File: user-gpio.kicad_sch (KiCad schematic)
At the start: 70 parts, among them J13 61232020621, J14 62704020621, J15 62703420621, J4 PMOD-2x6-artyA7_spacing, J5 PMOD-2x6-artyA7_spacing, Q10 BSS138PW, Q11 BSS138PW, Q12 BSS138PW, Q13 BSS138PW, Q14 BSS138PW, Q15 BSS138PW, Q8 BSS138PW, Q9 BSS138PW, SW2 CVS-08TB

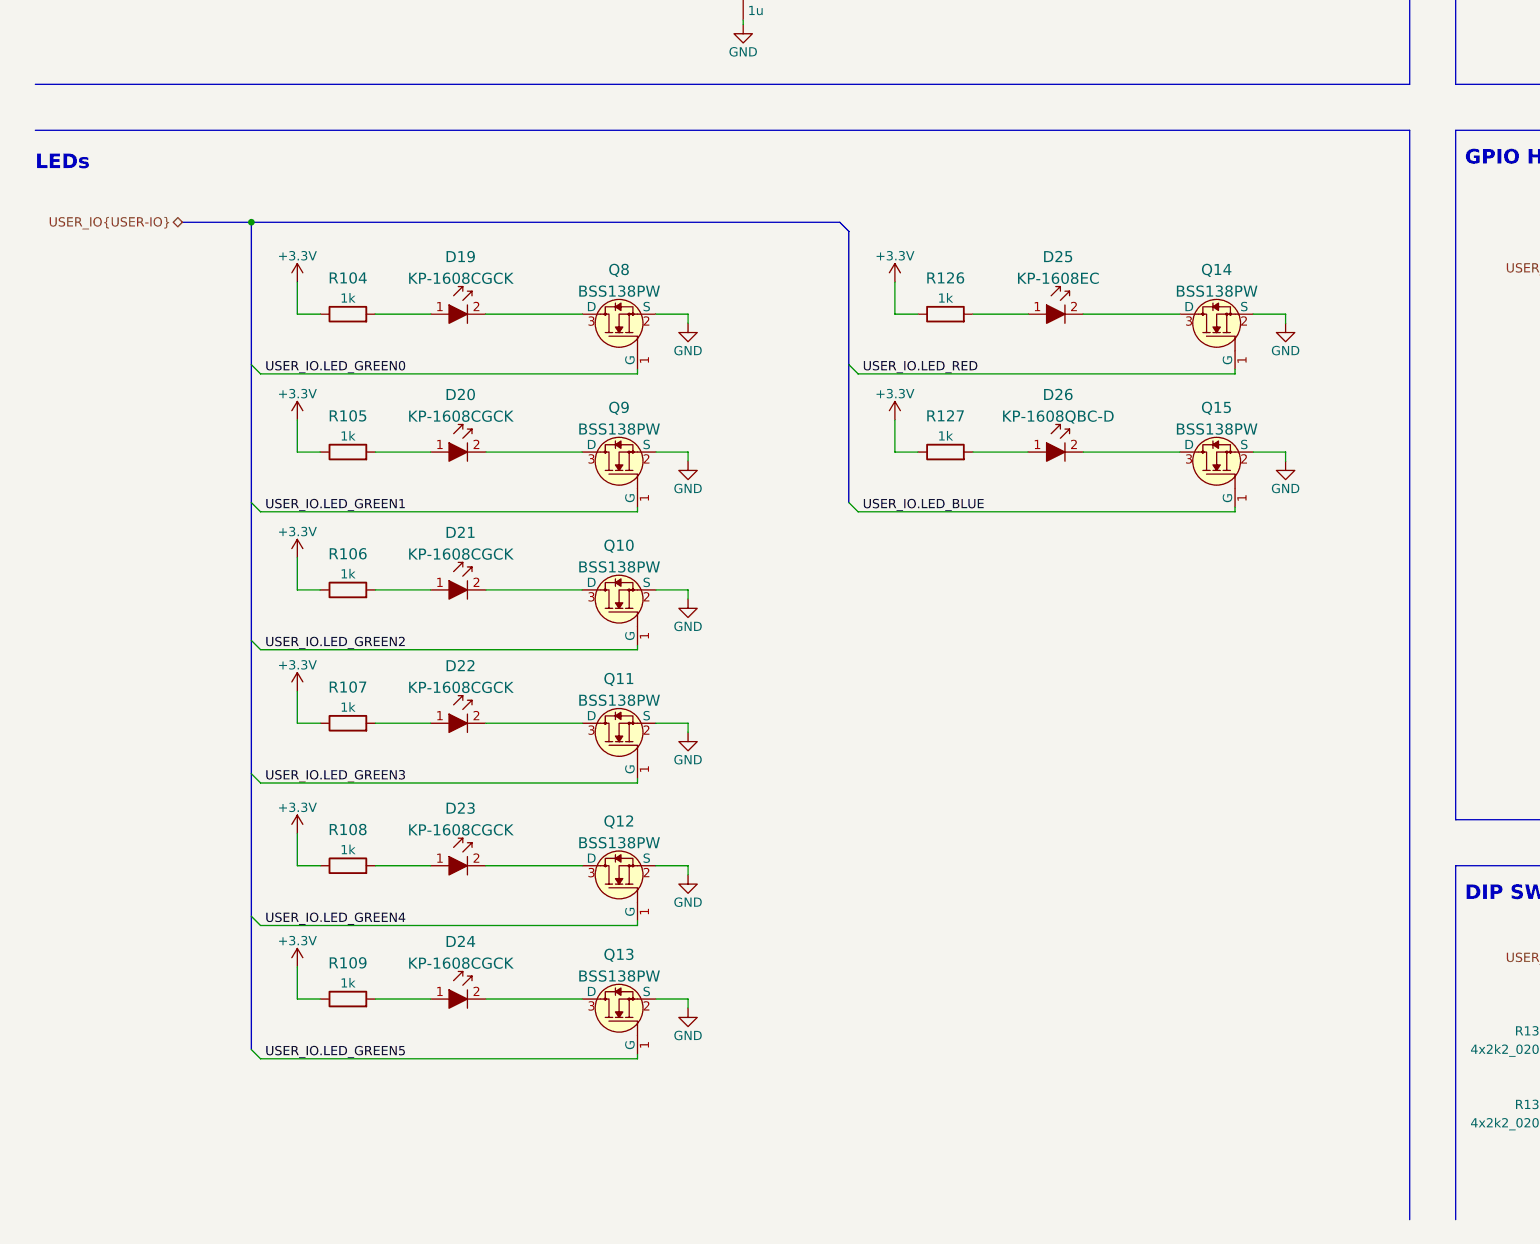
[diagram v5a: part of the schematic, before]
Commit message: Add fan headers
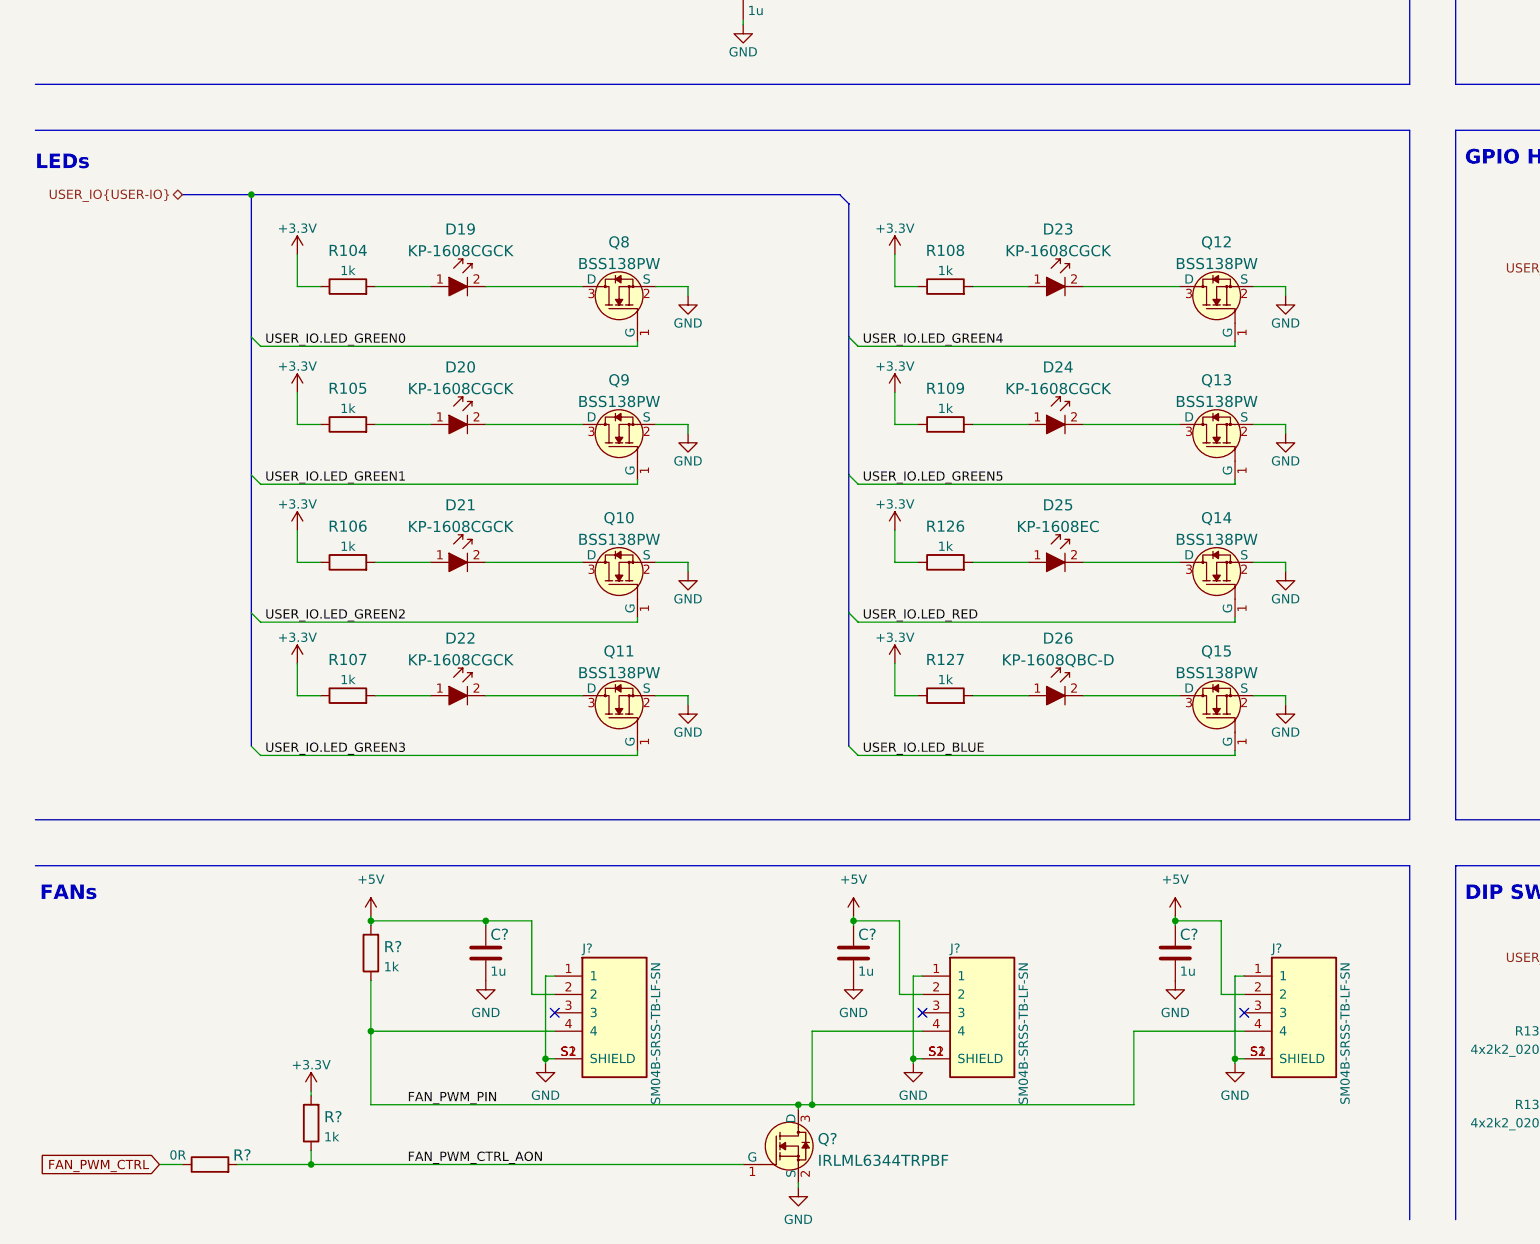
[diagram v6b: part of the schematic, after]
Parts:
- added C? (x3): C_1u_0402, antmicro-footprints:0402-cap, symbol antmicroCapacitors0402:C_1u_0402
- added J? (x3): SM04B-SRSS-TB-LF-SN, antmicro-footprints:SM04B-SRSS-TB-LF-SN, symbol antmicroRectangularConnectorsHeadersMalePins:SM04B-SRSS-TB-LF-SN
- added Q?: IRLML6344TRPBF, antmicro-footprints:SOT-23-3, symbol antmicroTransistorsFETsMOSFETsSingle:IRLML6344TRPBF
- added R?: R_0R_0402, antmicro-footprints:0402-res, symbol antmicroResistors0402:R_0R_0402
- added R? (x2): R_1k_0402, antmicro-footprints:0402-res, symbol antmicroResistors0402:R_1k_0402
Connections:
- net +3V3: now also R?.2
- net GND: now also C?.2, C?.2, C?.2, J?.1, J?.1, J?.1, J?.S1 (SHIELD), J?.S1 (SHIELD), J?.S1 (SHIELD), J?.S2 (SHIELD), J?.S2 (SHIELD), J?.S2 (SHIELD), Q?.2 (S)
- new net +5V: C?.1, C?.1, C?.1, J?.2, J?.2, J?.2, R?.2
- new net FAN_PWM_CTRL: R?.1
- new net FAN_PWM_CTRL_AON: Q?.1 (G), R?.1, R?.2
- new net FAN_PWM_PIN: J?.4, J?.4, J?.4, Q?.3 (D), R?.1
- no-connect marks 4 -> 7
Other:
- note added: "FANs"
- moved on the sheet: D19, D20, D21, D22, D23, D24, D25, D26, Q10, Q11, Q12, Q13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

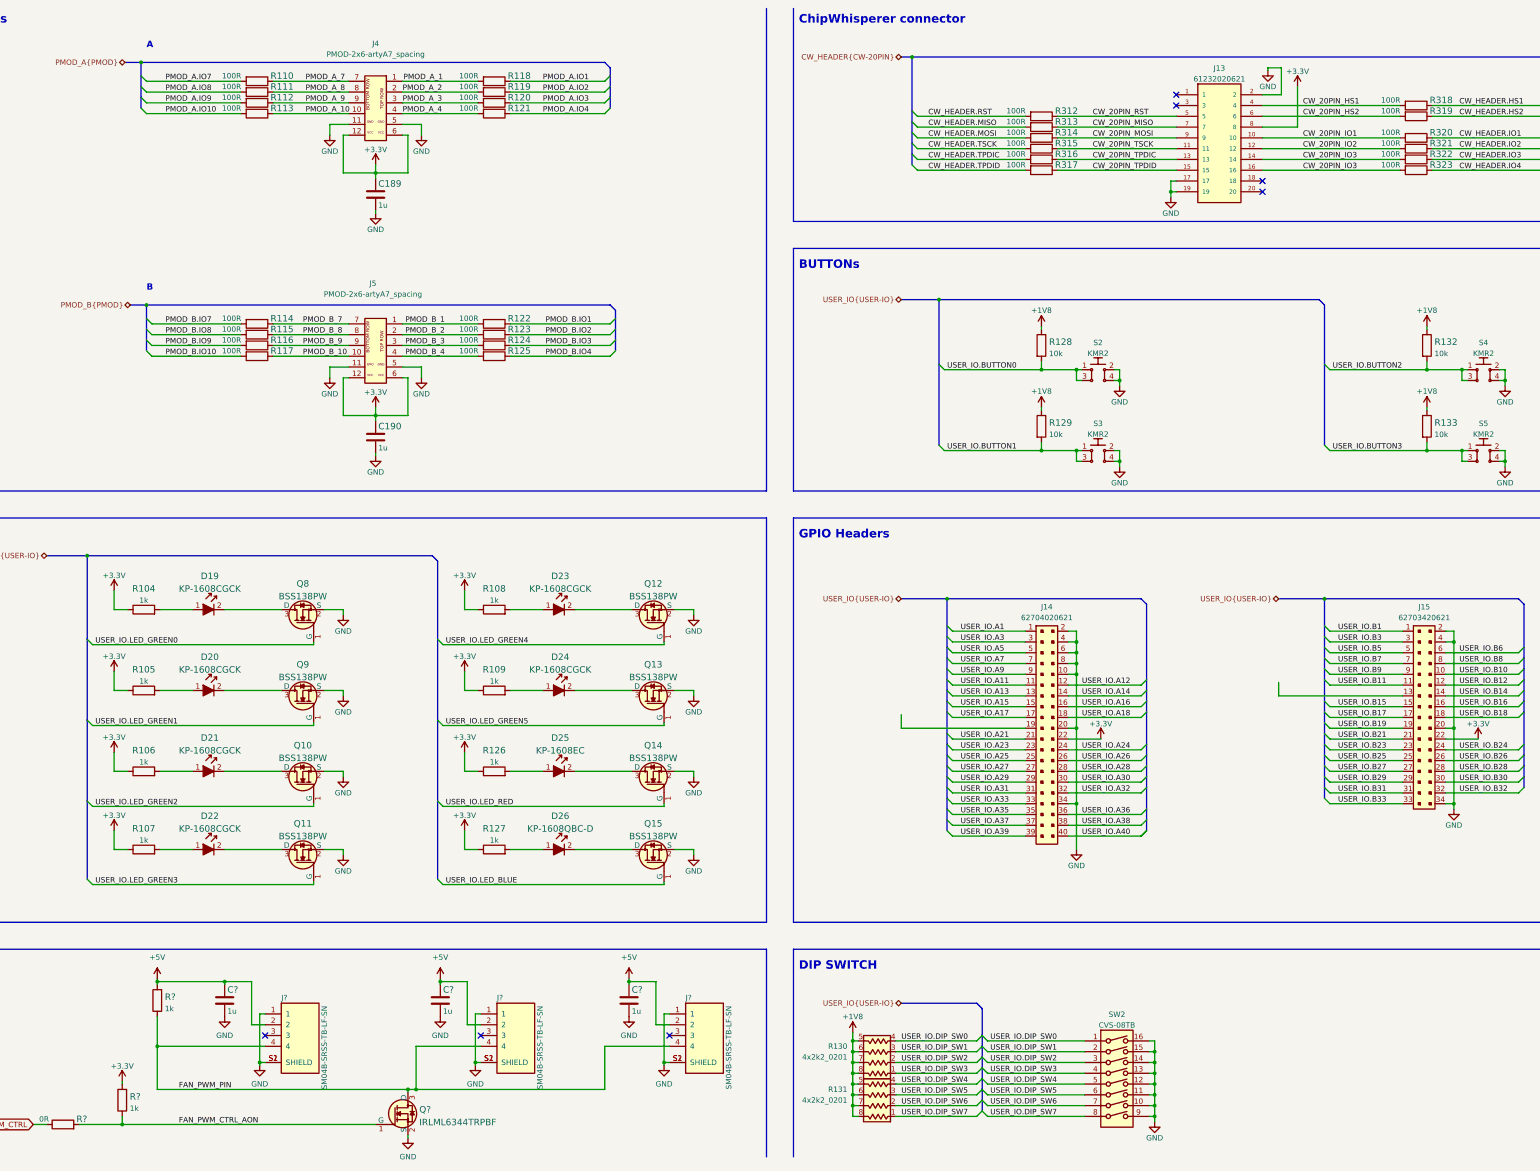
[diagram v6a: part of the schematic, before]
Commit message: Re-annotate the schematic. Export changes to PCB
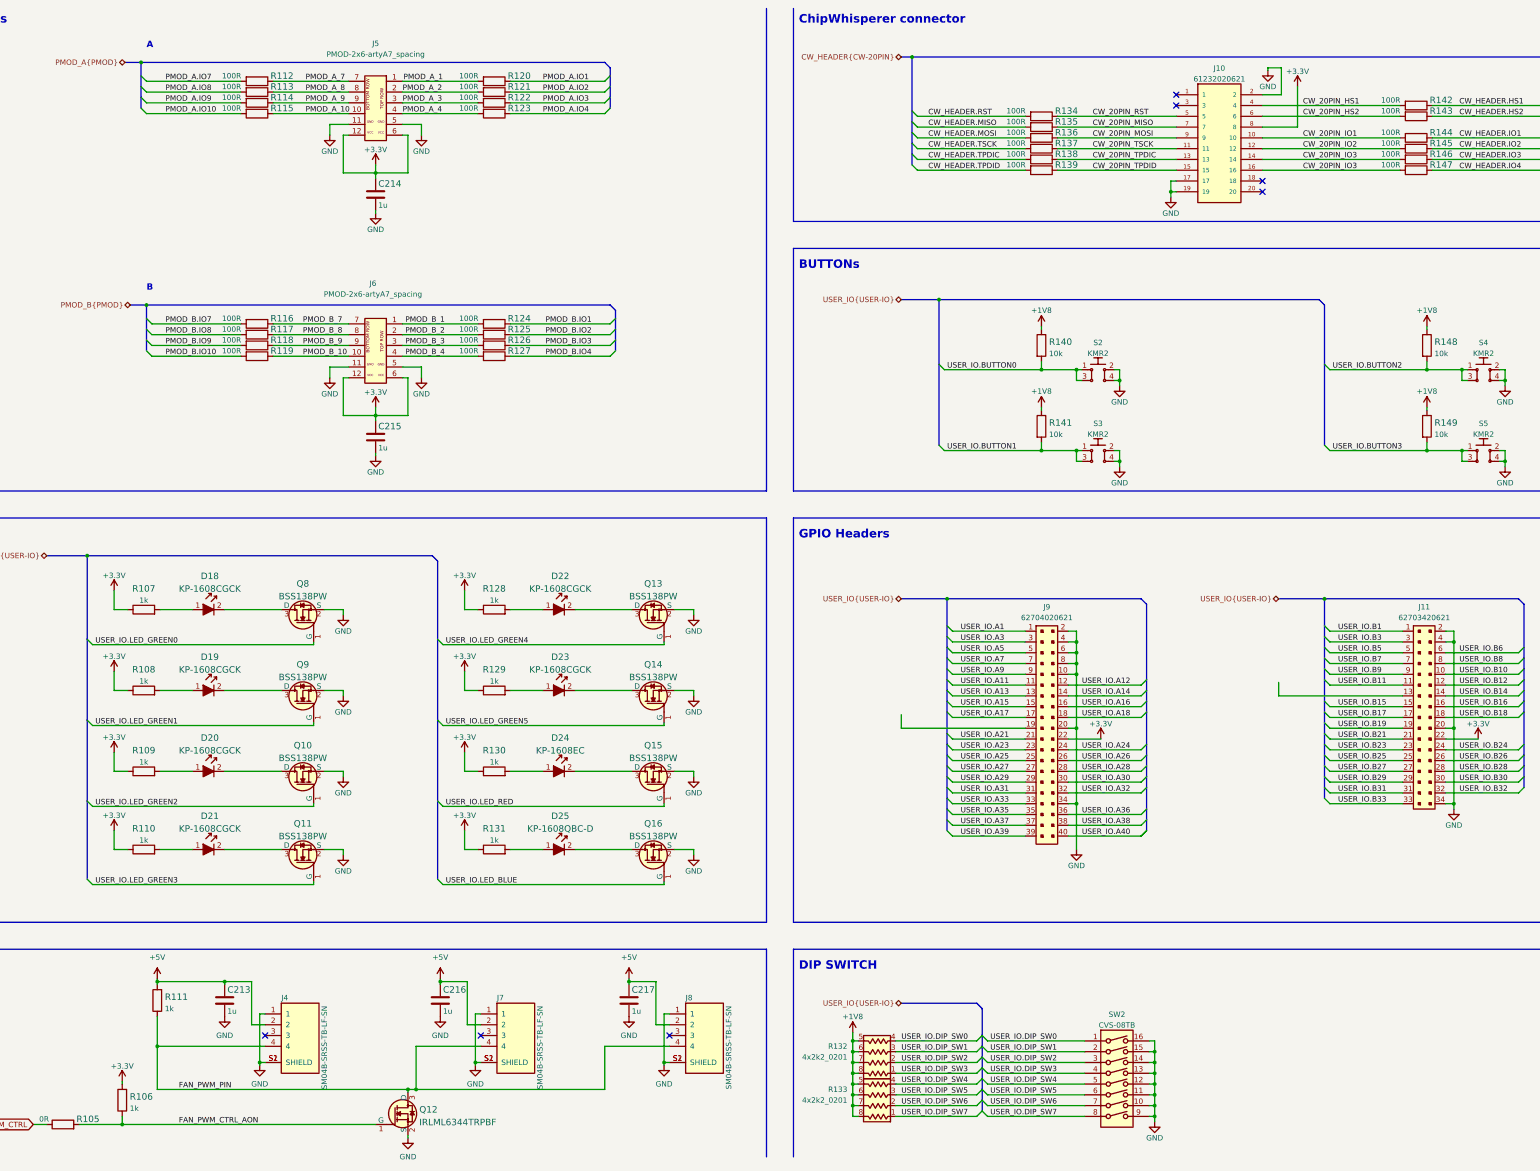
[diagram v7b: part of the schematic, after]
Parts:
- gave numbers to parts that had none: 10
- renumbered C189 to C214, C190 to C215, D19 to D18, D20 to D19, D21 to D20, D22 to D21, D23 to D22, D24 to D23, D25 to D24, D26 to D25, J13 to J10, J15 to J11, J4 to J5, J5 to J6, J14 to J9, Q12 to Q13, Q13 to Q14, Q14 to Q15, Q15 to Q16, R104 to R107, R105 to R108, R106 to R109, R107 to R110, R110 to R112, R111 to R113, R112 to R114, R113 to R115, R114 to R116, R115 to R117, R116 to R118, R117 to R119, R118 to R120, R119 to R121, R120 to R122, R121 to R123, R122 to R124, R123 to R125, R124 to R126, R125 to R127, R108 to R128, R109 to R129, R126 to R130, R127 to R131, R130 to R132, R131 to R133, R312 to R134, R313 to R135, R314 to R136, R315 to R137, R316 to R138, R317 to R139, R128 to R140, R129 to R141, R318 to R142, R319 to R143, R320 to R144, R321 to R145, R322 to R146, R323 to R147, R132 to R148, R133 to R149

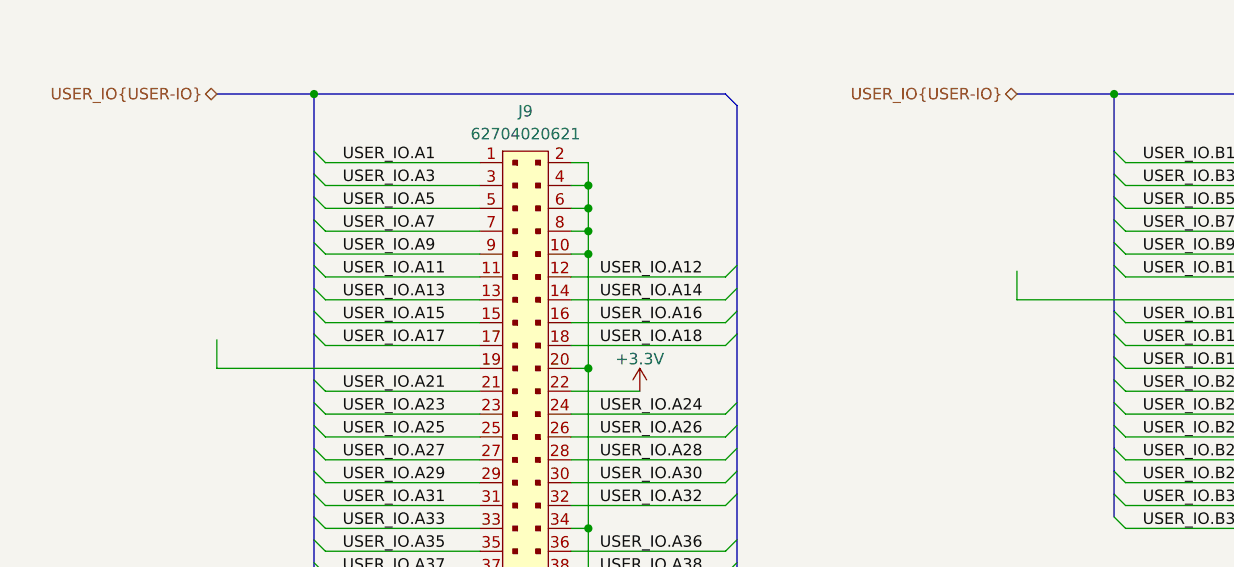
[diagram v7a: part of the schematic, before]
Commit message: Add VCC_USC_A/B labels, apply them to GPIO, FPGA power and SPI Flash
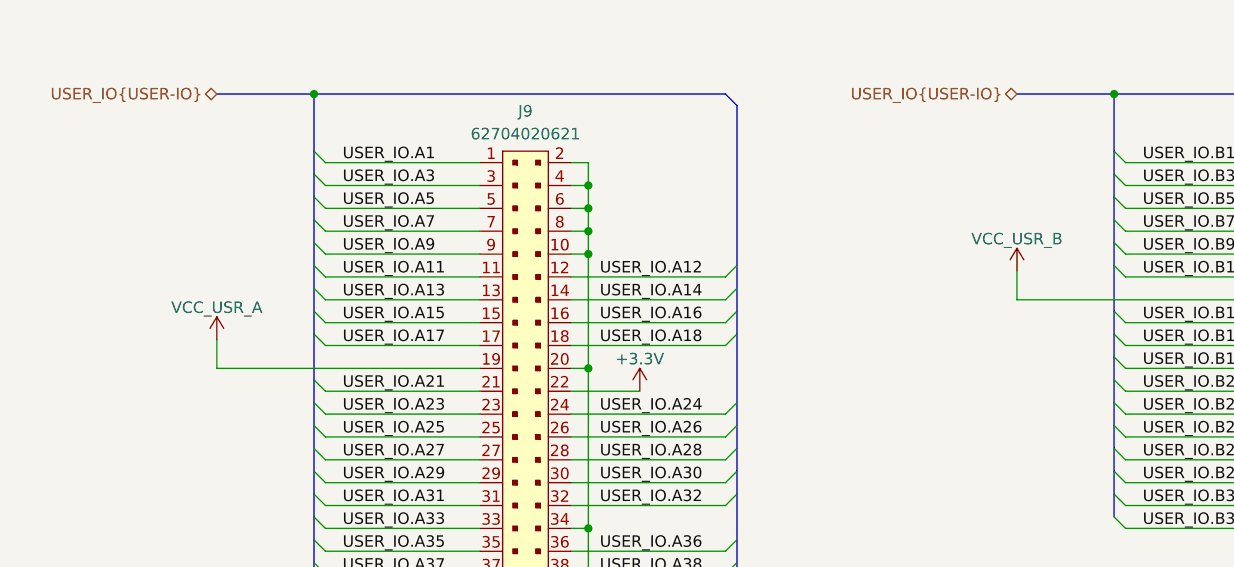
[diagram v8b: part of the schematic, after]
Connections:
- net VCC_USR_A: now reaches J9.19
- net VCC_USR_B: now reaches J11.13
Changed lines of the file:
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@@
     (pin "2")
+  )
+  (symbol (lib_id "antmicroPower:VCC_USR_A") (at 234.95 179.705 0) (mirror y) (unit 1)
+    (in_bom yes) (on_board yes) (fields_autoplaced)
+    (property "Reference" "#PWR?" (id 0) (at 234.95 183.515 0)
+      (effects (font (size 1.27 1.27)) hide)
+    )
+    (property "Value" "VCC_USR_A" (id 1) (at 234.95 176.1292 0))
+    (property "Footprint" "" (id 2) (at 234.95 179.705 0)
+      (effects (font (size 1.27 1.27)) hide)
+    )
+    (property "Datasheet" "" (id 3) (at 234.95 179.705 0)
+      (effects (font (size 1.27 1.27)) hide)
+    )
+    (pin "1")
   )
   (symbol (lib_id "power:GND") (at 179.07 262.255 0) (unit 1)
@@
       (effects (font (size 1.27 1.27)) hide)
     )
+    (pin "1")
+  )
+  (symbol (lib_id "antmicroPower:VCC_USR_B") (at 323.85 172.085 0) (mirror y) (unit 1)
+    (in_bom yes) (on_board yes) (fields_autoplaced)
+    (property "Reference" "#PWR?" (id 0) (at 323.85 175.895 0)
+      (effects (font (size 1.27 1.27)) hide)
+    )
+    (property "Value" "VCC_USR_B" (id 1) (at 323.85 168.5092 0))
+    (property "Footprint" "" (id 2) (at 323.85 172.085 0)
+      (effects (font (size 1.27 1.27)) hide)
+    )
+    (property "Datasheet" "" (id 3) (at 323.85 172.085 0)
+      (effects (font (size 1.27 1.27)) hide)
+    )
